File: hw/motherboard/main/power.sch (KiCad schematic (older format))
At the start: 11 parts, among them J6 5V power in, U3 LP5907MFX-3_3_NOPB, U4 TLV75533PDBV

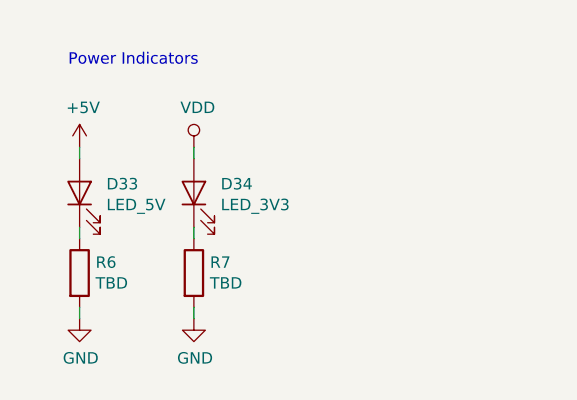
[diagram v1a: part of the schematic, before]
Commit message: Add missing component values.
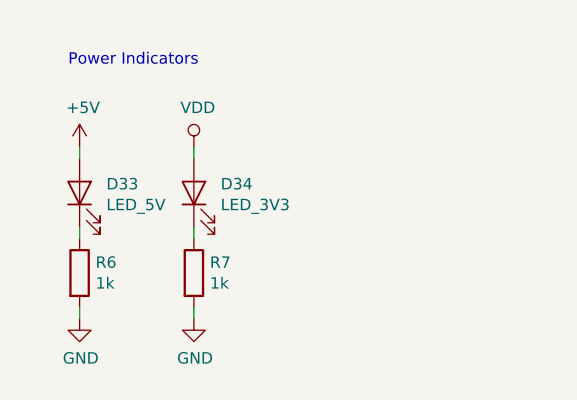
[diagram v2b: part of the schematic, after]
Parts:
- R6, R7: value TBD -> 1k
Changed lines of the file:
@@
 AR Path="/5F4CCA9E/5F6A0E68" Ref="R6"  Part="1"
 F 0 "R6" H 1320 3246 50  0000 L CNN
-F 1 "TBD" H 1320 3155 50  0000 L CNN
+F 1 "1k" H 1320 3155 50  0000 L CNN
 F 2 "Resistor_SMD:R_0805_2012Metric" V 1180 3200 50  0001 C CNN
 F 3 "~" H 1250 3200 50  0001 C CNN
@@
 AR Path="/5F4CCA9E/5F6A0E83" Ref="R7"  Part="1"
 F 0 "R7" H 1820 3246 50  0000 L CNN
-F 1 "TBD" H 1820 3155 50  0000 L CNN
+F 1 "1k" H 1820 3155 50  0000 L CNN
 F 2 "Resistor_SMD:R_0805_2012Metric" V 1680 3200 50  0001 C CNN
 F 3 "~" H 1750 3200 50  0001 C CNN

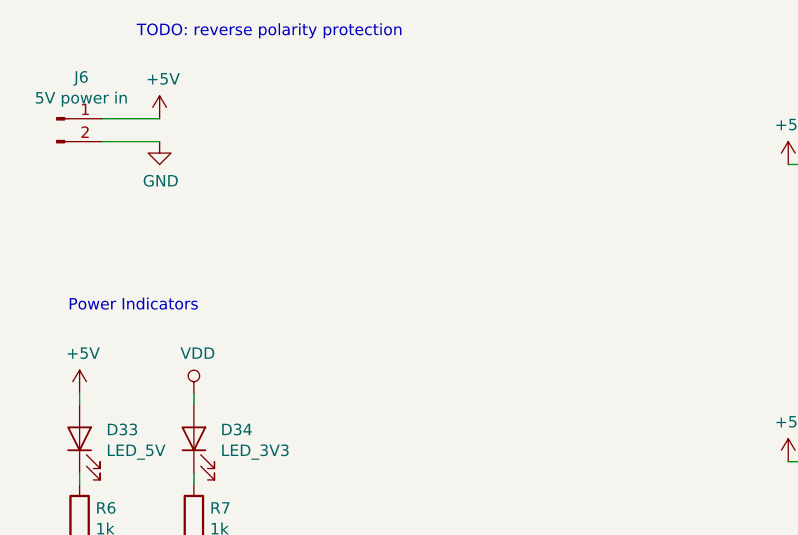
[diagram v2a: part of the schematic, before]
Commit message: Add reverse polarity protection to +5V input. Bump revision number to 1.2.
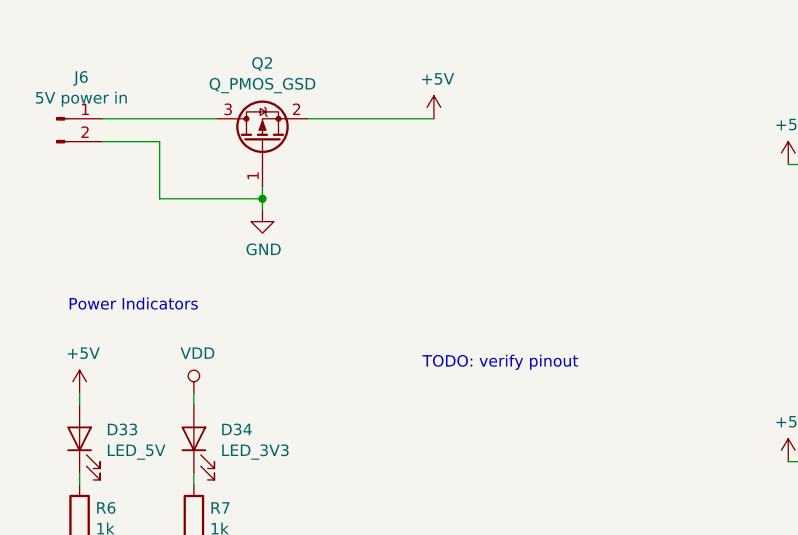
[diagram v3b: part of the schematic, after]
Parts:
- added Q2: Q_PMOS_GSD, Package_TO_SOT_SMD:SOT-23, symbol Device:Q_PMOS_GSD
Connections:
- net +5V: now also Q2.2 (S); no longer J6.1 (Pin_1)
- net GND: now also Q2.1 (G)
- new net: J6.1 (Pin_1), Q2.3 (D)
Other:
- note added: "TODO: verify pinout"
- note removed: "TODO: reverse polarity protection"
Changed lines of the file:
@@
 Title "KAPINE Motherboard"
 Date "2020-09-02"
-Rev "1.1"
+Rev "1.2"
 Comp "Verneri Hirvonen"
 Comment1 ""
@@
 $EndComp
 Wire Wire Line
-	1350 1450 1600 1450
+	1350 1450 1850 1450
 Wire Wire Line
 	1350 1550 1600 1550
-$Comp
-L power:GND #PWR021
-U 1 1 5F4BFEB4
-P 1600 1550
-F 0 "#PWR021" H 1600 1300 50  0001 C CNN
-F 1 "GND" H 1605 1377 50  0000 C CNN
-F 2 "" H 1600 1550 50  0001 C CNN
-F 3 "" H 1600 1550 50  0001 C CNN
-	1    1600 1550
-	1    0    0    -1
-$EndComp
 $Comp
 L power:+5V #PWR019
 U 1 1 5F4C0045
-P 1600 1450
-F 0 "#PWR019" H 1600 1300 50  0001 C CNN
-F 1 "+5V" H 1615 1623 50  0000 C CNN
-F 2 "" H 1600 1450 50  0001 C CNN
-F 3 "" H 1600 1450 50  0001 C CNN
-	1    1600 1450
+P 2800 1450
+F 0 "#PWR019" H 2800 1300 50  0001 C CNN
+F 1 "+5V" H 2815 1623 50  0000 C CNN
+F 2 "" H 2800 1450 50  0001 C CNN
+F 3 "" H 2800 1450 50  0001 C CNN
+	1    2800 1450
 	1    0    0    -1
 $EndComp
@@
 Wire Wire Line
 	5400 2050 6000 2050
-Text Notes 1500 1100 0    50   ~ 0
-TODO: reverse polarity protection
 Text Notes 7400 1450 0    50   ~ 0
 Power Label Descriptions:\n* +5V -- external 5V input for regulators\n* VDD -- regulated 3.3V Digital logic power\n* VDDA -- regulated 3.3V Analog reference voltage
@@
 Text Notes 1200 2300 0    50   ~ 0
 Power Indicators
+Text Notes 2750 2550 0    50   ~ 0
+TODO: verify pinout
+$Comp
+L Device:Q_PMOS_GSD Q2
+U 1 1 5F519668
+P 2050 1550
+F 0 "Q2" V 2392 1550 50  0000 C CNN
+F 1 "Q_PMOS_GSD" V 2301 1550 50  0000 C CNN
+F 2 "Package_TO_SOT_SMD:SOT-23" H 2250 1650 50  0001 C CNN
+F 3 "~" H 2050 1550 50  0001 C CNN
+	1    2050 1550
+	0    -1   -1   0
+$EndComp
+$Comp
+L power:GND #PWR021
+U 1 1 5F51B2CA
+P 2050 1850
+F 0 "#PWR021" H 2050 1600 50  0001 C CNN
+F 1 "GND" H 2055 1677 50  0000 C CNN
+F 2 "" H 2050 1850 50  0001 C CNN
+F 3 "" H 2050 1850 50  0001 C CNN
+	1    2050 1850
+	1    0    0    -1
+$EndComp
+Wire Wire Line
+	2250 1450 2800 1450
+Wire Wire Line
+	2050 1750 2050 1800
+Wire Wire Line
+	2050 1800 1600 1800
+Wire Wire Line
+	1600 1800 1600 1550
+Connection ~ 2050 1800
+Wire Wire Line
+	2050 1800 2050 1850
 $EndSCHEMATC
